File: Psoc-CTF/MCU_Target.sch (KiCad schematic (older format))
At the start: 41 parts

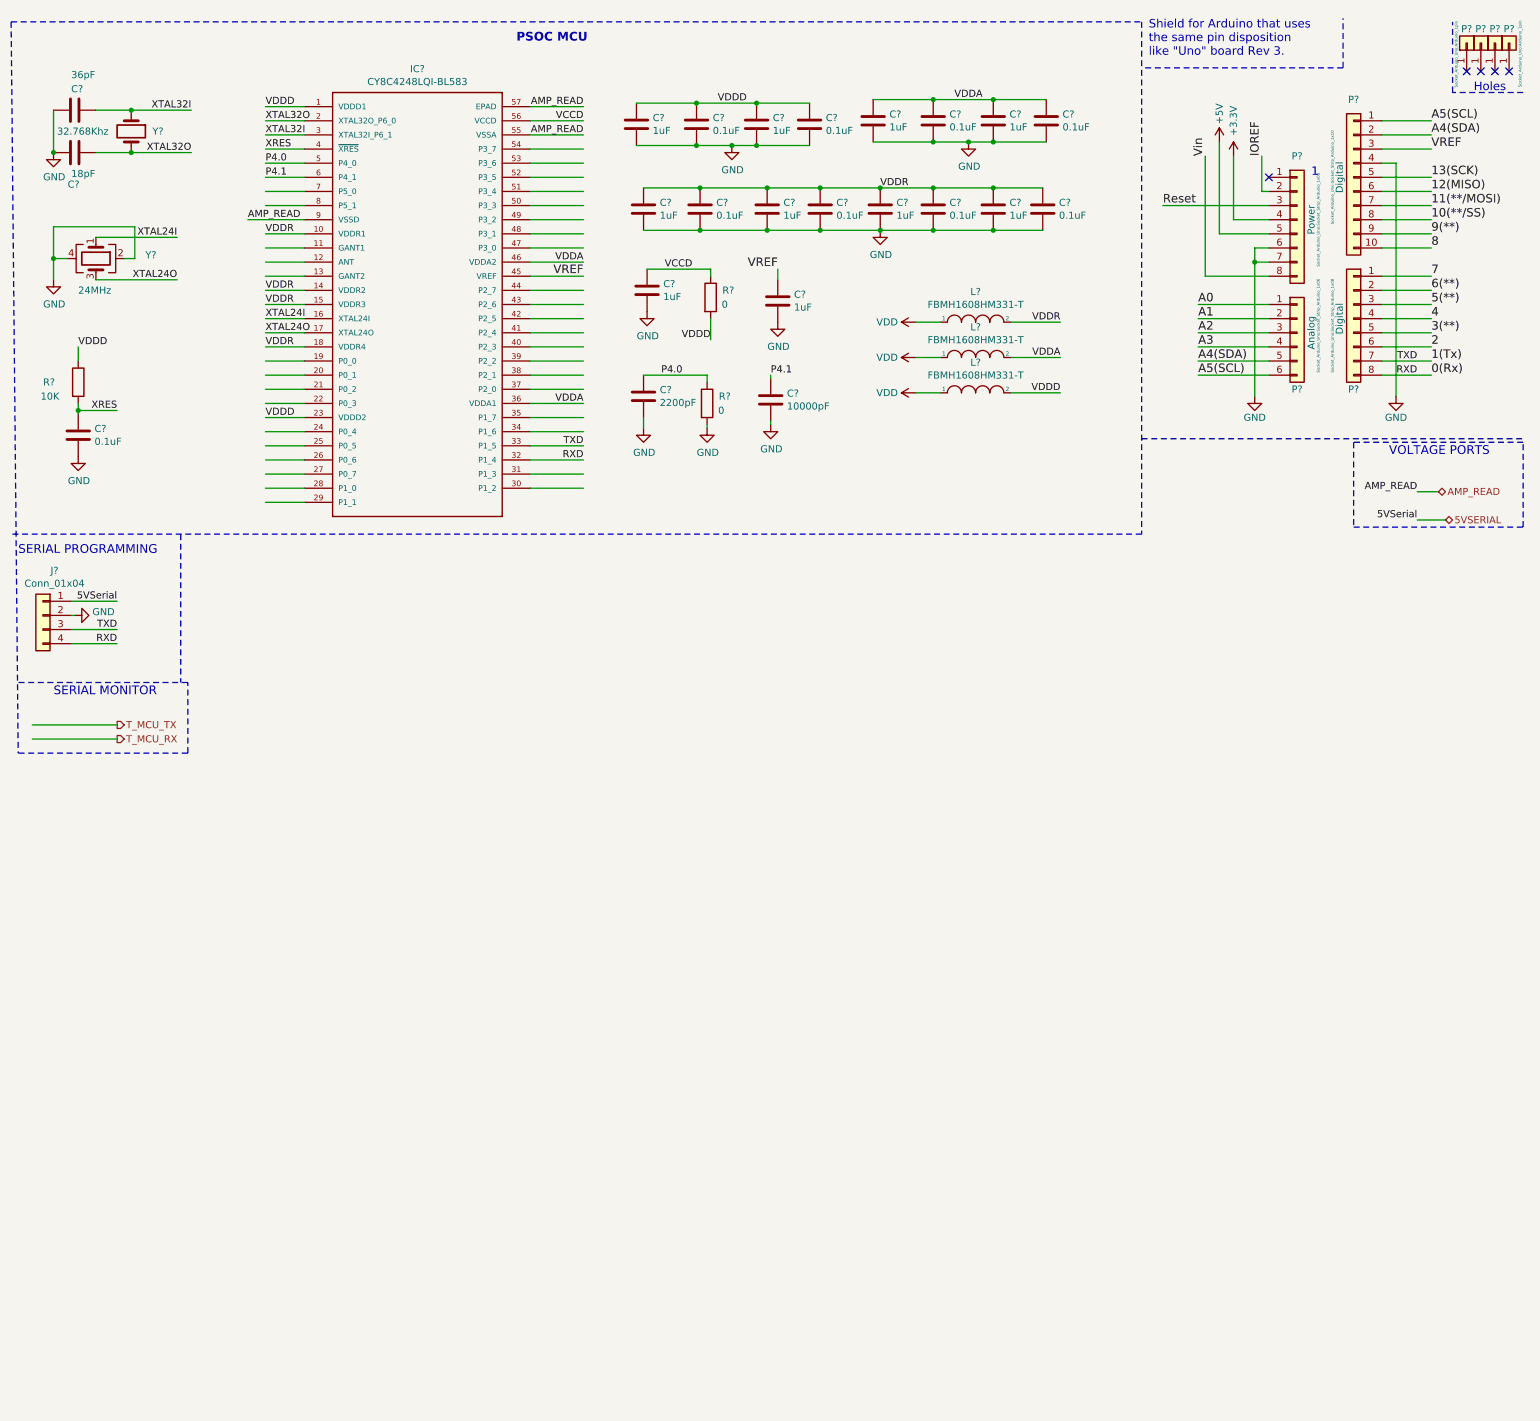
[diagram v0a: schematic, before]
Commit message: Generación de lista de materiales
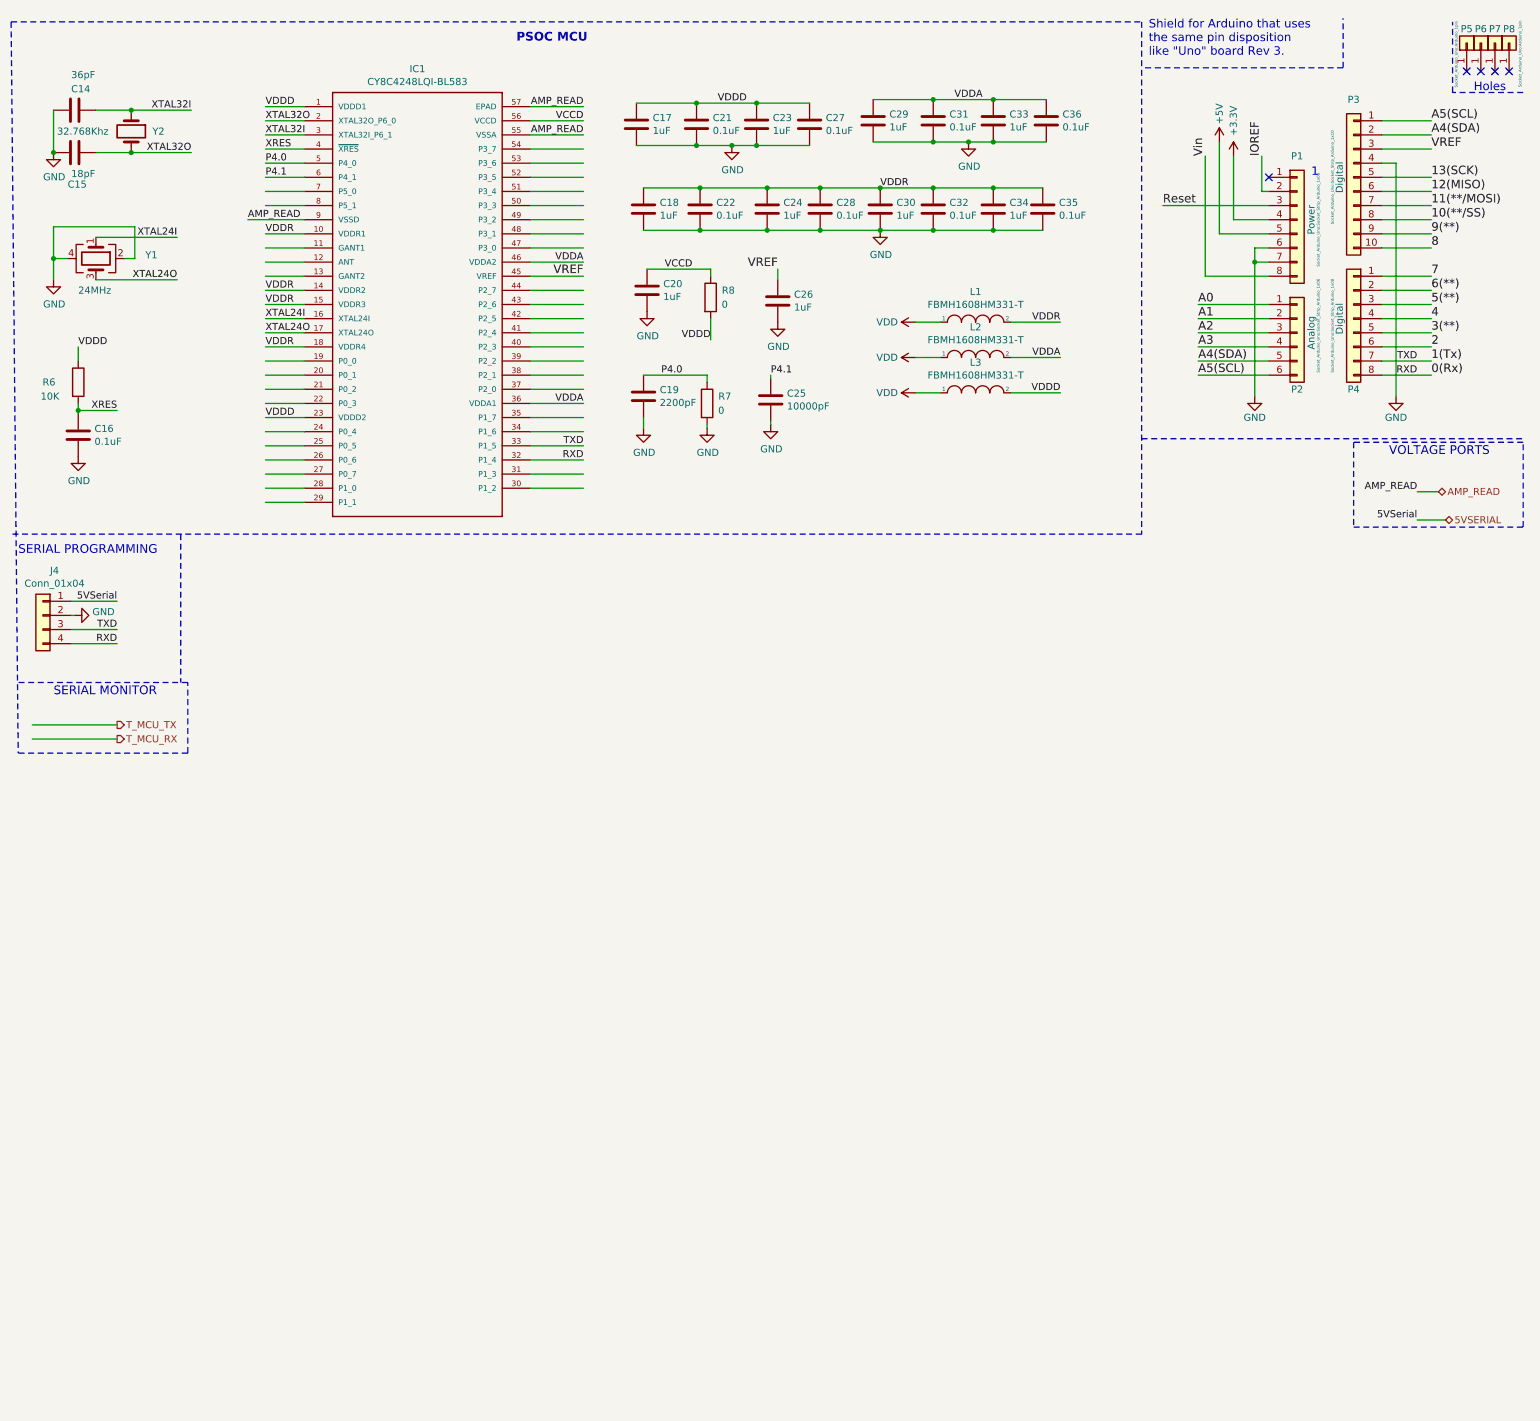
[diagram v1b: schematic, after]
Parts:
- gave numbers to parts that had none: 41

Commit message: Archivo Cache para cadlab
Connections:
- net labels added: +12V
- net labels removed: IOREF, Reset
- wire segments 164 -> 165
- no-connect marks 5 -> 6
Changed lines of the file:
@@
 Comment4 ""
 $EndDescr
-Text Label 8950 1475 1    60   ~ 0
-Vin
-Text Label 9350 1475 1    60   ~ 0
-IOREF
 Text Label 8900 2525 0    60   ~ 0
 A0
@@
 	1    0    0    -1
 $EndComp
-Text Label 8650 1825 0    60   ~ 0
-Reset
 $Comp
 L power:+3.3V #PWR?
@@
 	9925 850  9925 500
 Wire Wire Line
-	9350 1475 9350 1725
-Wire Wire Line
-	9350 1725 9400 1725
-Wire Wire Line
 	9400 1925 9150 1925
-Wire Wire Line
-	9400 2025 9050 2025
 Wire Wire Line
 	9400 2325 8950 2325
@@
 Connection ~ 9300 2225
 Wire Wire Line
-	8950 2325 8950 1475
-Wire Wire Line
-	9050 2025 9050 1375
+	8950 2325 8950 1600
 Wire Wire Line
 	9150 1925 9150 1475
@@
 L power:GND #PWR?
 U 1 1 6215E689
-P 7275 1375
+P 7275 1400
 AR Path="/6215E689" Ref="#PWR?"  Part="1"
 AR Path="/62149449/6215E689" Ref="#PWR043"  Part="1"
-F 0 "#PWR043" H 7275 1125 50  0001 C CNN
-F 1 "GND" H 7280 1202 50  0000 C CNN
-F 2 "" H 7275 1375 50  0001 C CNN
-F 3 "" H 7275 1375 50  0001 C CNN
-	1    7275 1375
+F 0 "#PWR043" H 7275 1150 50  0001 C CNN
+F 1 "GND" H 7280 1227 50  0000 C CNN
+F 2 "" H 7275 1400 50  0001 C CNN
+F 3 "" H 7275 1400 50  0001 C CNN
+	1    7275 1400
 	1    0    0    -1
 $EndComp
@@
 L power:GND #PWR?
 U 1 1 6215E6C3
-P 5000 2575
+P 5000 2600
 AR Path="/6215E6C3" Ref="#PWR?"  Part="1"
 AR Path="/62149449/6215E6C3" Ref="#PWR034"  Part="1"
-F 0 "#PWR034" H 5000 2325 50  0001 C CNN
-F 1 "GND" H 5005 2402 50  0000 C CNN
-F 2 "" H 5000 2575 50  0001 C CNN
-F 3 "" H 5000 2575 50  0001 C CNN
-	1    5000 2575
+F 0 "#PWR034" H 5000 2350 50  0001 C CNN
+F 1 "GND" H 5005 2427 50  0000 C CNN
+F 2 "" H 5000 2600 50  0001 C CNN
+F 3 "" H 5000 2600 50  0001 C CNN
+	1    5000 2600
 	1    0    0    -1
 $EndComp
@@
 	6900 2650 7075 2650
 Wire Wire Line
-	6900 2900 7075 2900
-Wire Wire Line
-	6900 3150 7075 3150
-Wire Wire Line
 	7575 2650 7925 2650
 Wire Wire Line
@@
 Text Notes 10250 3600 0    62   ~ 0
 VOLTAGE PORTS
+Text HLabel 8950 1475 1    50   Input ~ 0
+Vin
+Wire Wire Line
+	5000 2575 5000 2600
+Wire Wire Line
+	7075 2900 6900 2900
+Wire Wire Line
+	6900 3150 7075 3150
+Wire Wire Line
+	7275 1375 7275 1400
+$Comp
+L power:+12V #PWR0102
+U 1 1 62130D8D
+P 8950 1600
+F 0 "#PWR0102" H 8950 1450 50  0001 C CNN
+F 1 "+12V" V 8965 1728 50  0000 L CNN
+F 2 "" H 8950 1600 50  0001 C CNN
+F 3 "" H 8950 1600 50  0001 C CNN
+	1    8950 1600
+	0    -1   -1   0
+$EndComp
+Connection ~ 8950 1600
+Wire Wire Line
+	8950 1600 8950 1475
+Text Label 8650 1825 0    50   ~ 0
+XRES
+NoConn ~ 9400 1725
+Wire Wire Line
+	9050 1375 9050 2025
+Wire Wire Line
+	9050 2025 9400 2025
 $EndSCHEMATC

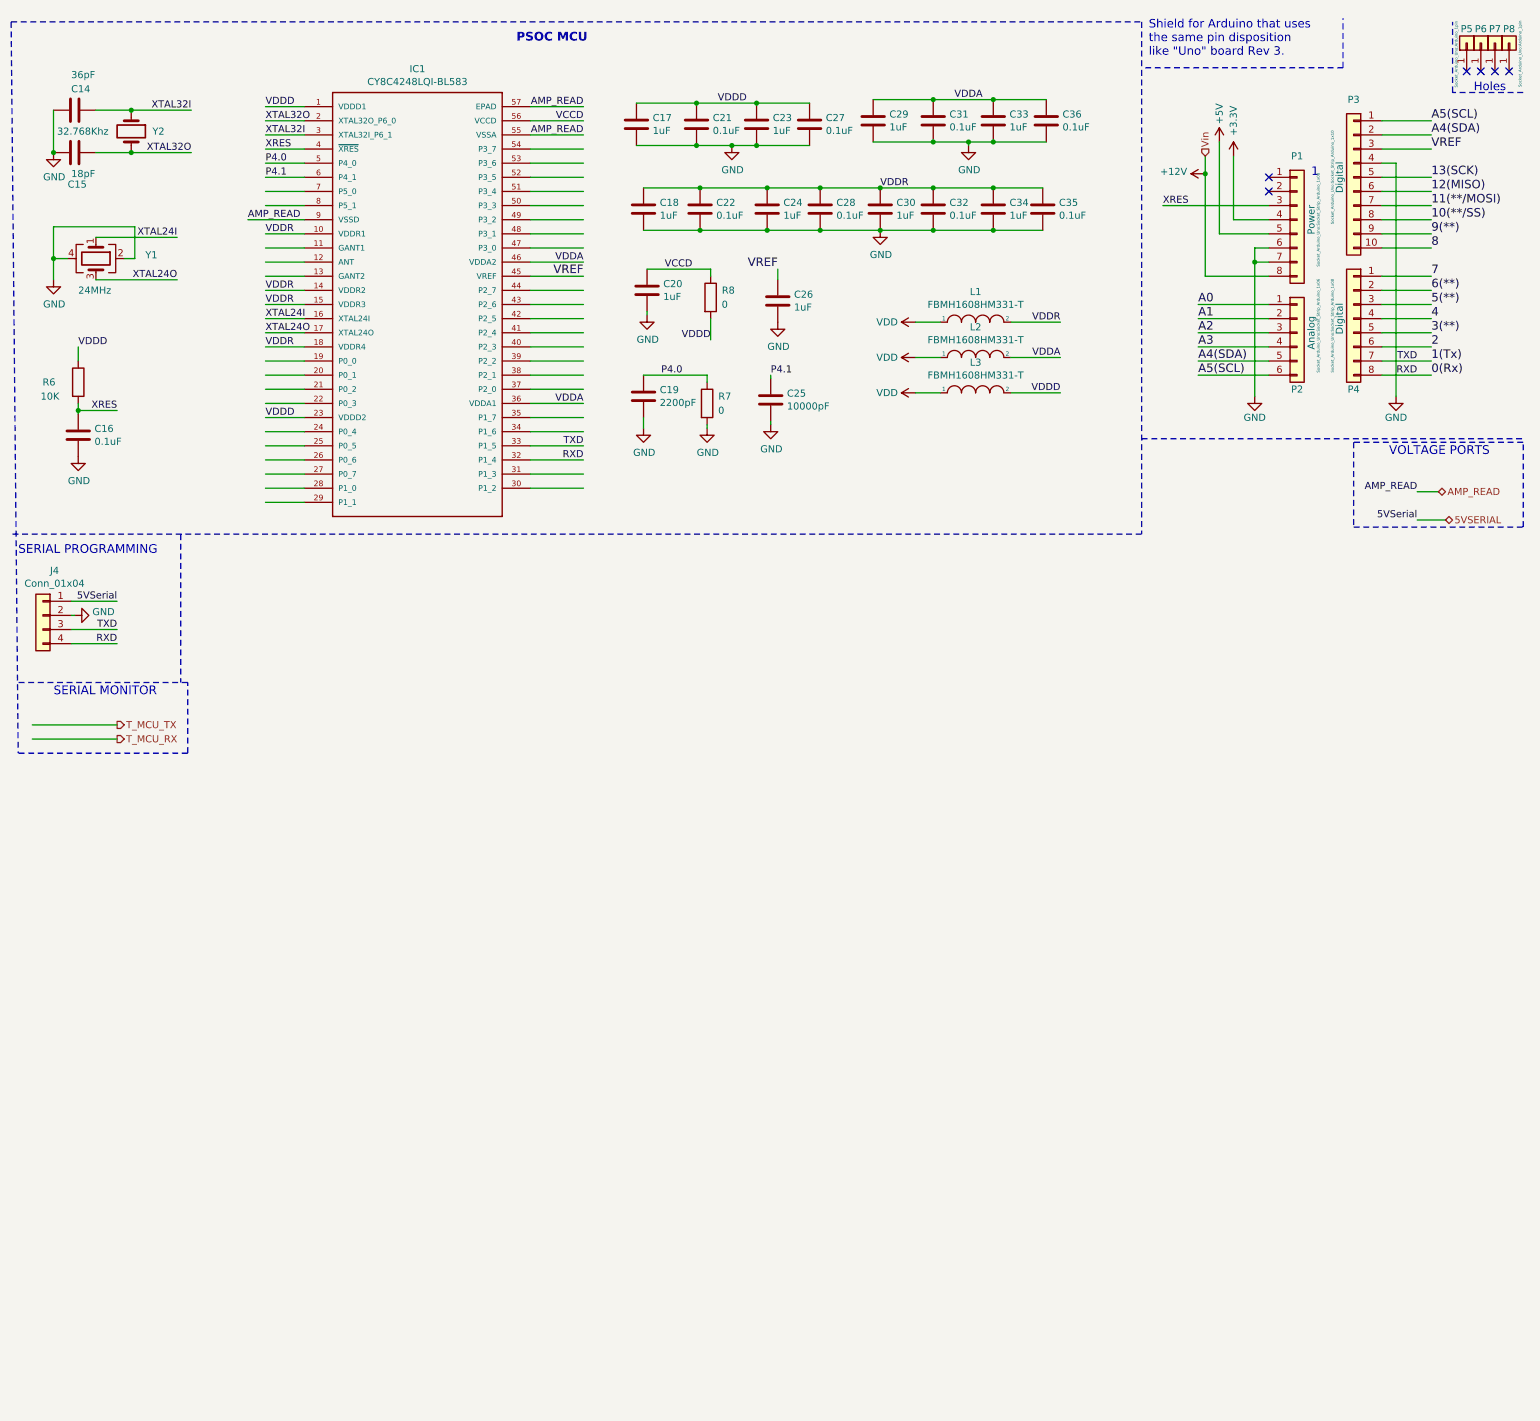
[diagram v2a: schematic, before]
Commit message: Se retira las memorias flash y Ram por spi y se coloca una F-RAM por i2c
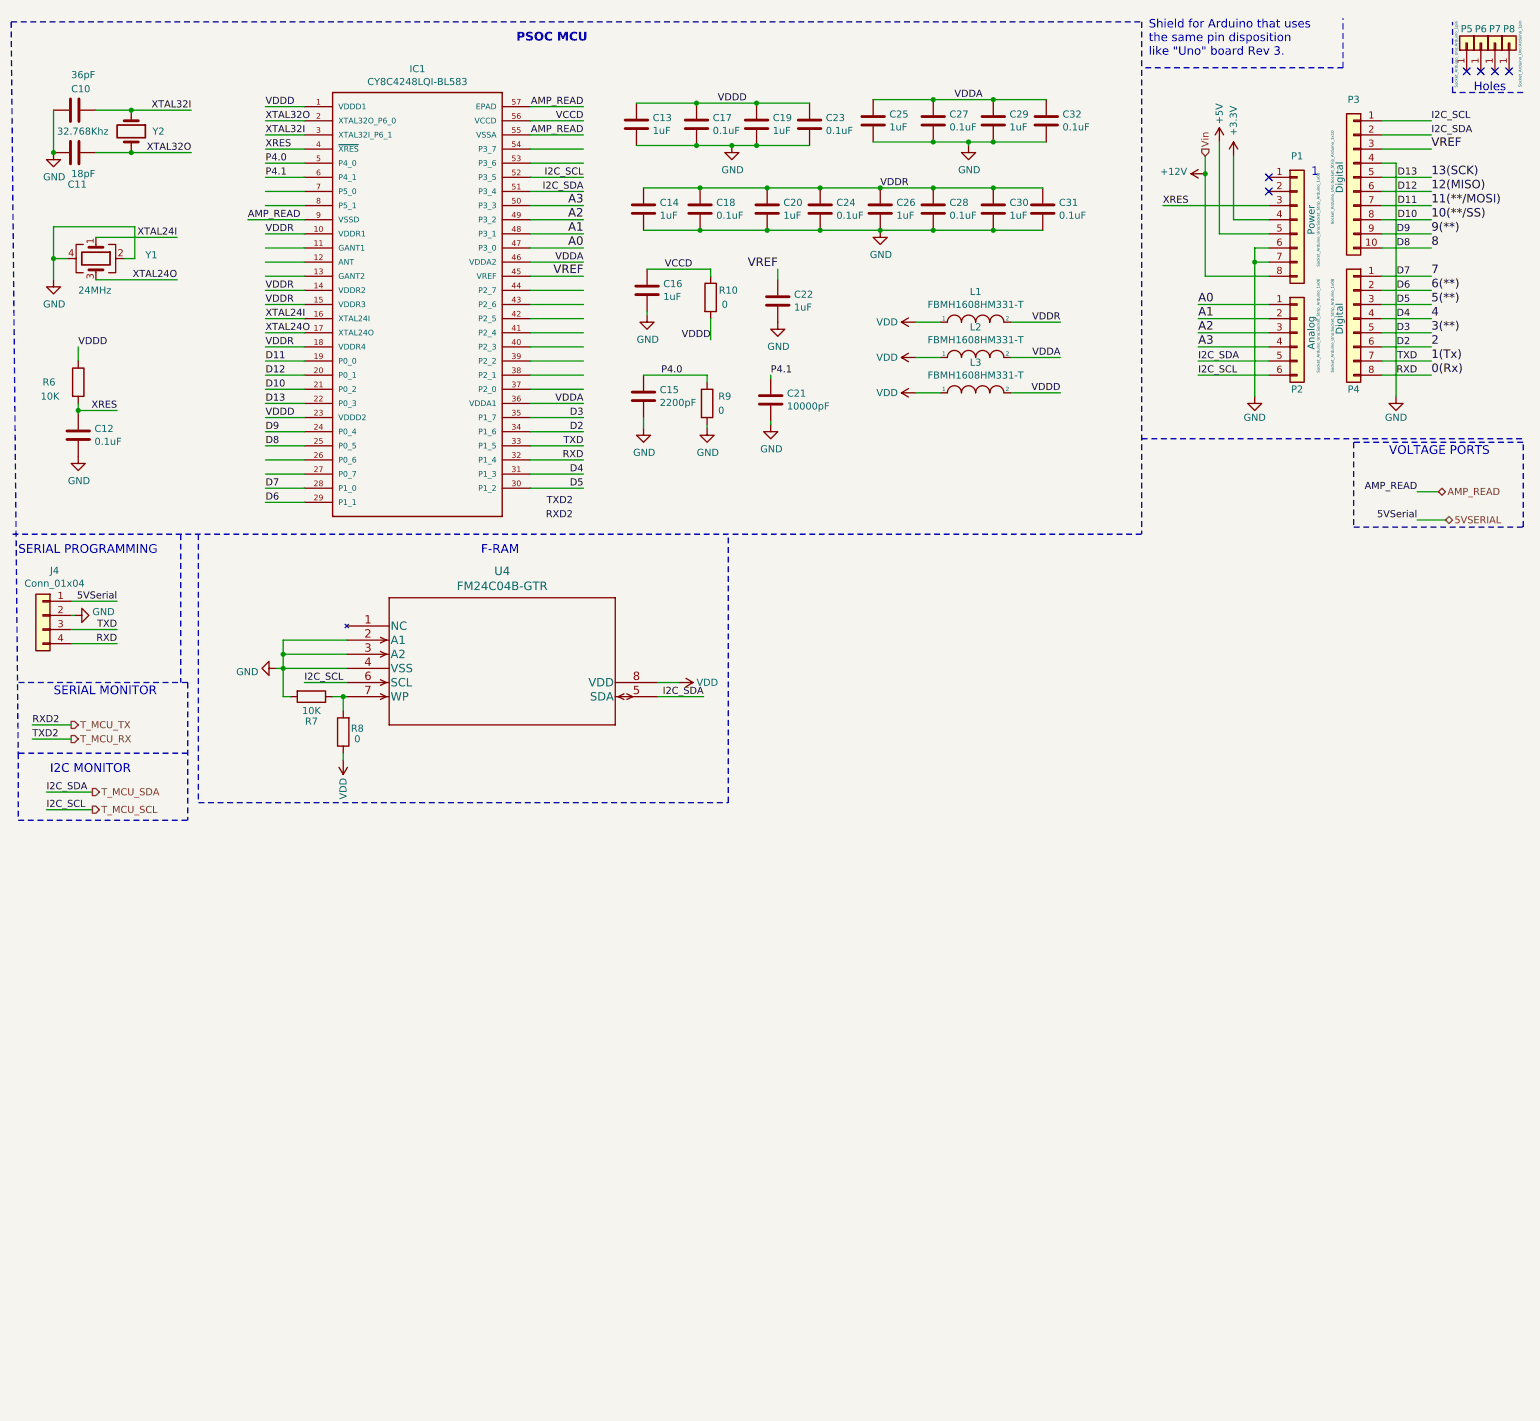
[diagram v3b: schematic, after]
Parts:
- added R7: 10K, Resistor_SMD:R_0603_1608Metric_Pad0.98x0.95mm_HandSolder, symbol Device:R
- added R8: 0, Resistor_SMD:R_0603_1608Metric_Pad0.98x0.95mm_HandSolder, symbol Device:R
- added U4: FM24C04B-GTR, Psoc-CTF:23LC1024-E&slash_SN, symbol FM24C04B:FM24C04B-GTR
- J4: footprint (none) -> Connector_PinHeader_2.54mm:PinHeader_1x04_P2.54mm_Vertical
- Y1: footprint (none) -> Crystal:Crystal_SMD_3225-4Pin_3.2x2.5mm
- Y2: footprint (none) -> Crystal:Crystal_SMD_EuroQuartz_EQ161-2Pin_3.2x1.5mm_HandSoldering
- renumbered C14 to C10, C15 to C11, C16 to C12, C17 to C13, C18 to C14, C19 to C15, C20 to C16, C21 to C17, C22 to C18, C23 to C19, C24 to C20, C25 to C21, C26 to C22, C27 to C23, C28 to C24, C29 to C25, C30 to C26, C31 to C27, C32 to C28, C33 to C29, C34 to C30, C35 to C31, C36 to C32, R8 to R10, R7 to R9
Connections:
- net labels added: D10, D11, D12, D13, D2, D3, D4, D5, D6, D7, D8, D9, I2C_SCL, I2C_SDA, RXD2, TXD2, T_MCU_SCL, T_MCU_SDA
- net labels removed: A4(SDA), A5(SCL)
- wire segments 165 -> 182
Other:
- note added: "F-RAM"
- note added: "I2C MONITOR"
